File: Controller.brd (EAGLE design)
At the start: 125 x 65 mm, 38 parts, among them SW1 MULTICOLOR_BUTTON, SW2 MULTICOLOR_BUTTON, SW3 MULTICOLOR_BUTTON, SW4 MULTICOLOR_BUTTON, SW5 MULTICOLOR_BUTTON, SW6 MULTICOLOR_BUTTON, SW7 MULTICOLOR_BUTTON, SW8 MULTICOLOR_BUTTON, U1 ATMEGA328-PU, U2 DRV5053VAQLPGM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

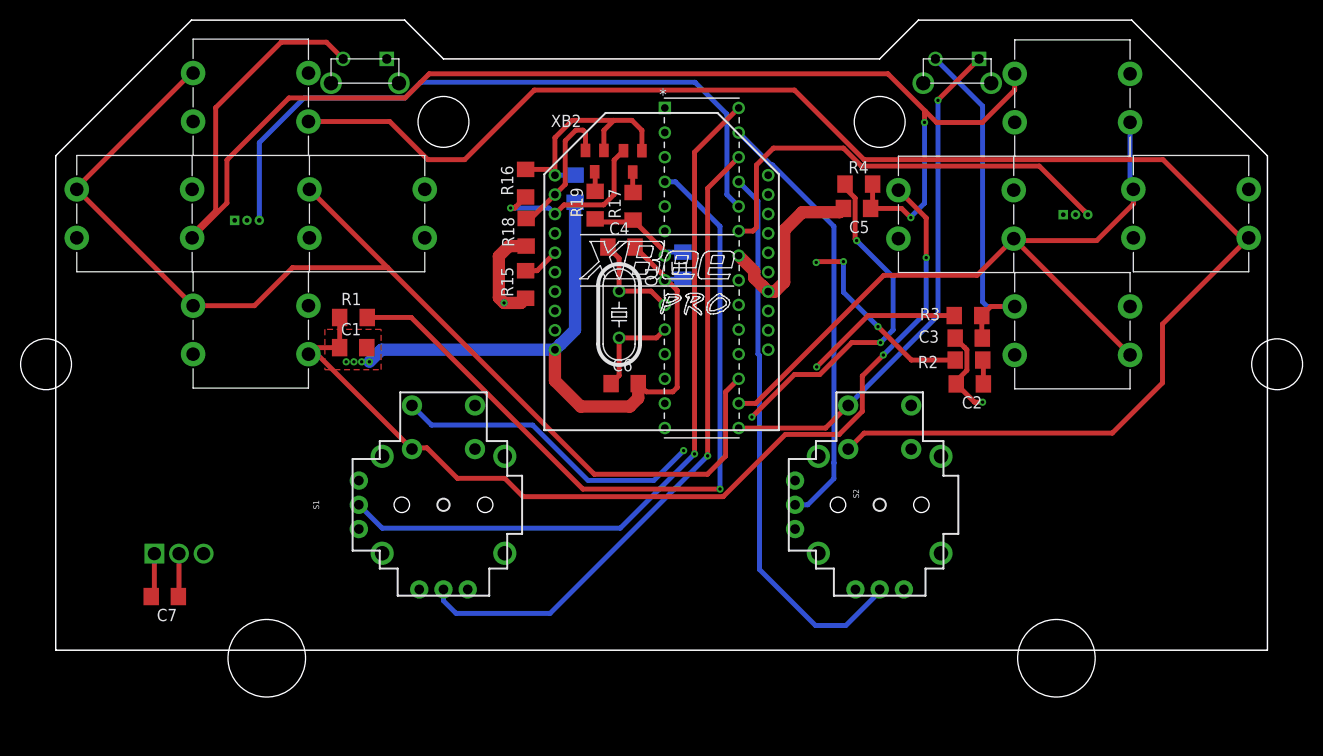
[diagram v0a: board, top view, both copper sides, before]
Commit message: added 5V regulator
Still need to add BMS circuitry and switch
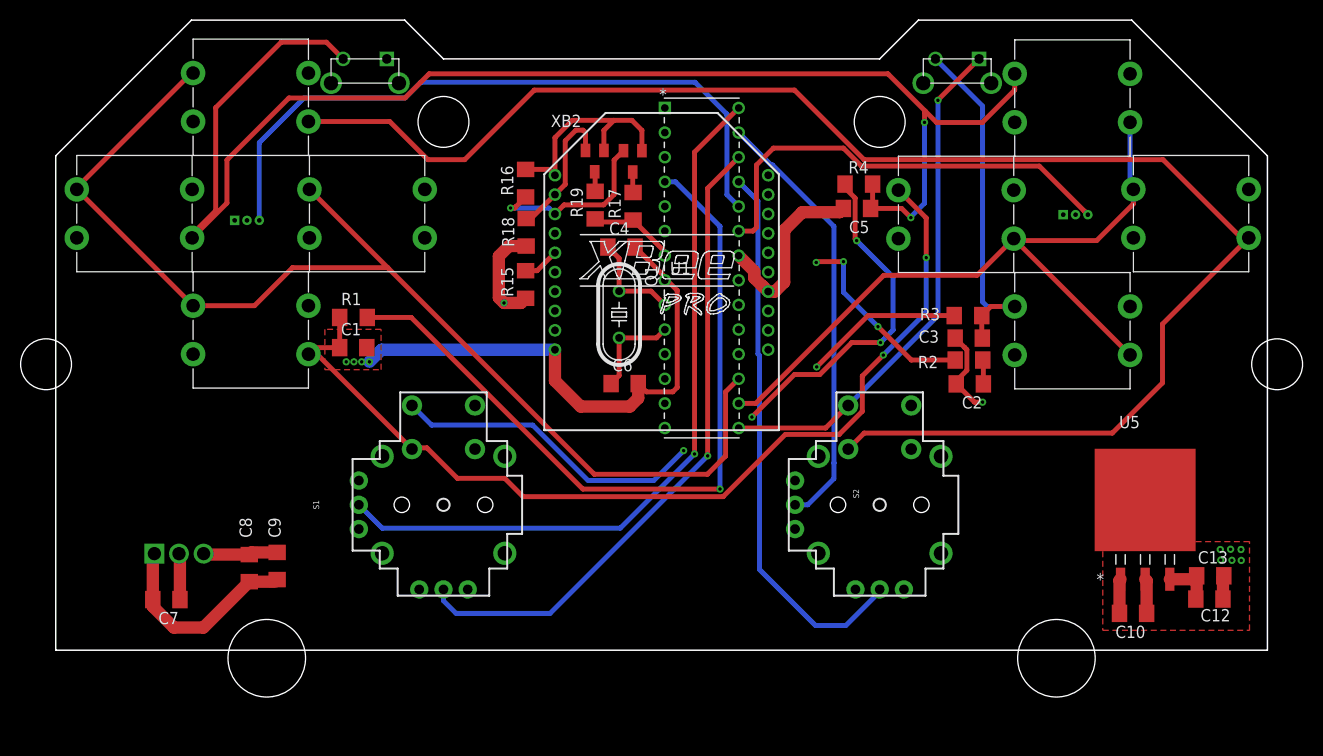
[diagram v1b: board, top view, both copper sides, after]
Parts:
- added C10, C12: 10u, rcl:C1206
- added C13: 0.1u, rcl:C1206
- added U5: LM1085ISX-5.0/NOPBTS3B-L, Controller:TS3B-L
- moved C8 54.5 mm to (20.0, 8.47), flipped to the top
- moved C9 49.6 mm to (22.8, 8.69), flipped to the top
- moved C7 0.35 mm to (11.4, 5.22)
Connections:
- new net VBAT: C12.1, C13.1, U5.3
- net +3V3: no longer C9.1
- net +5V: now also C10.1, C9.1, U5.2
- net GND: now also C10.2, C12.2, C13.2, U5.1
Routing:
- net +5V: track 91.4 -> 100.7 mm
- net VBAT: track 0.00 -> 5.36 mm
- net GND: track 115.5 -> 120.2 mm, vias 5 -> 11
- net +3V3: track 109.1 -> 107.4 mm

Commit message: rerouted so we only have 2 layers, added PWM pin
Need to add battery switch,indicator Vbat pins
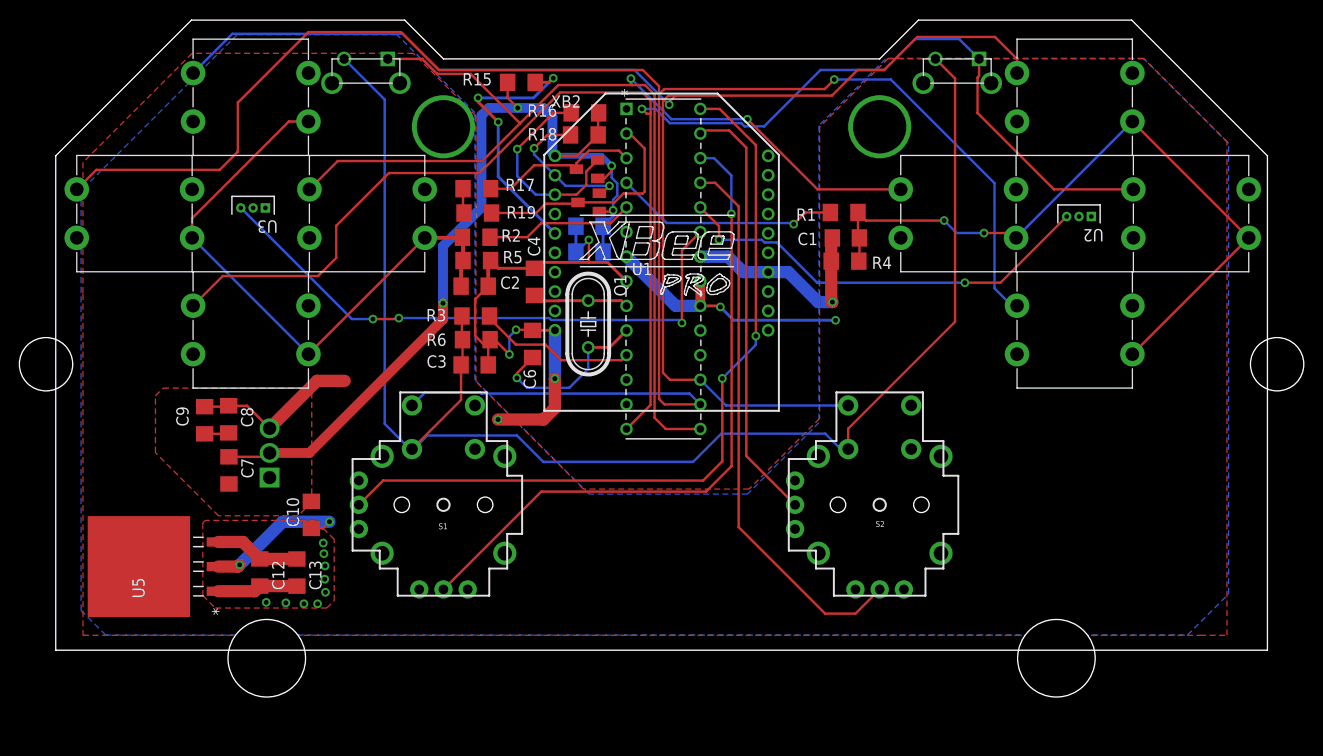
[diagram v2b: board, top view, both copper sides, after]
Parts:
- added C11: 0.1u, rcl:C1206
- added R5, R6: 100k, rcl:R1206
- C5: value 0.1u -> 10U
- moved U5 104.1 mm to (8.53, 8.62), turned to 90 degrees
- moved C12 98.0 mm to (21.1, 8.02), turned to 270 degrees
- moved SW1 97.7 mm to (117.0, 45.0)
- moved C13 94.2 mm to (24.9, 8.01), turned to 270 degrees
- moved SW2 88.3 mm to (105.0, 33.0)
- moved U3 87.4 mm to (19.1, 45.6), flipped to the top
- moved C10 85.4 mm to (26.4, 14.0), turned to 90 degrees
- moved SW8 85.0 mm to (20.0, 57.0), turned to 0 degrees
- moved U2 83.3 mm to (104.3, 44.7), flipped to the top
- moved SW7 74.0 mm to (32.0, 45.0), turned to 0 degrees
- moved R2 52.4 mm to (43.4, 42.6), turned to 0 degrees
- moved C2 52.1 mm to (43.2, 37.6), turned to 0 degrees
- moved C1 52.1 mm to (81.5, 42.5), turned to 180 degrees
- moved R1 51.8 mm to (81.3, 45.2), turned to 180 degrees
- moved C3 51.0 mm to (43.2, 29.4), turned to 0 degrees
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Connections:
- removed net $NC2: S2.B2A, SW2.4, SW6.4
- removed net AREF: U1.21
- removed net AVCC: U1.20
- removed net C4: R4.2, U1.14
- removed net N$C1: C1.1, R1.1, S1.B2A, SW1.4, SW5.4
- removed net N$C4: C5.1, R4.1, SW4.4, SW8.4, U$6.P$2
- new net $NC1: C1.1, R1.1, R4.1, SW1.4, SW2.4, SW5.4, SW6.4
- new net PWM: U1.12
- new net R4: S2.B1A, SW6.2, SW8.2, U1.17
- net +3V3: now also C11.1, C5.1
- net +5V: now also U1.20, U1.21
- net GND: now also C11.2, R4.2, R5.2, R6.2
- net N$C2: now also R5.1, SW3.4, SW4.4, SW7.4, SW8.4
- net N$C3: now also R6.1, S1.B2A, S2.B2A, U$6.P$2; no longer SW3.4, SW7.4
- net R1: now also U$4.P$1, U1.14; no longer SW2.2, SW4.2, U1.17
- net R2: now also U$6.P$1, U1.15; no longer SW6.2, SW8.2, U1.16
- net R3: now also SW2.2, SW4.2, U1.16; no longer S2.B1A, U$4.P$1, U$6.P$1, U1.15
- net RX: now also U1.2
- net TX: now also U1.3
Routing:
- net $NC2: track 161.8 -> 0.00 mm
- net N$C4: track 150.6 -> 0.00 mm, vias 2 -> 0
- net R4: track 0.00 -> 145.3 mm, vias 0 -> 1
- net N$C1: track 100.4 -> 0.00 mm, vias 2 -> 0
- net $NC1: track 0.00 -> 73.4 mm, vias 0 -> 2
- net R3: track 129.8 -> 193.2 mm, vias 2 -> 1
- net N$C2: track 2.49 -> 61.2 mm
- net N$C3: track 97.1 -> 154.8 mm
- net C1: track 78.4 -> 23.3 mm
- net R2: track 74.7 -> 128.7 mm, vias 0 -> 2
- net C4: track 44.8 -> 0.00 mm, vias 3 -> 0
- net R1: track 120.2 -> 159.7 mm, vias 0 -> 1
- net +5V: track 100.7 -> 62.4 mm, vias 0 -> 4
- net C2: track 50.0 -> 15.4 mm, vias 3 -> 0
- net GND: track 120.2 -> 92.3 mm, vias 11 -> 15
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- added copper zone on layer 1, net +5V
- added copper zone on layer 16, net GND
- removed copper zone on layer 2, net +5V
- removed copper zone on layer 15, net GND

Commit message: Added switch and LED
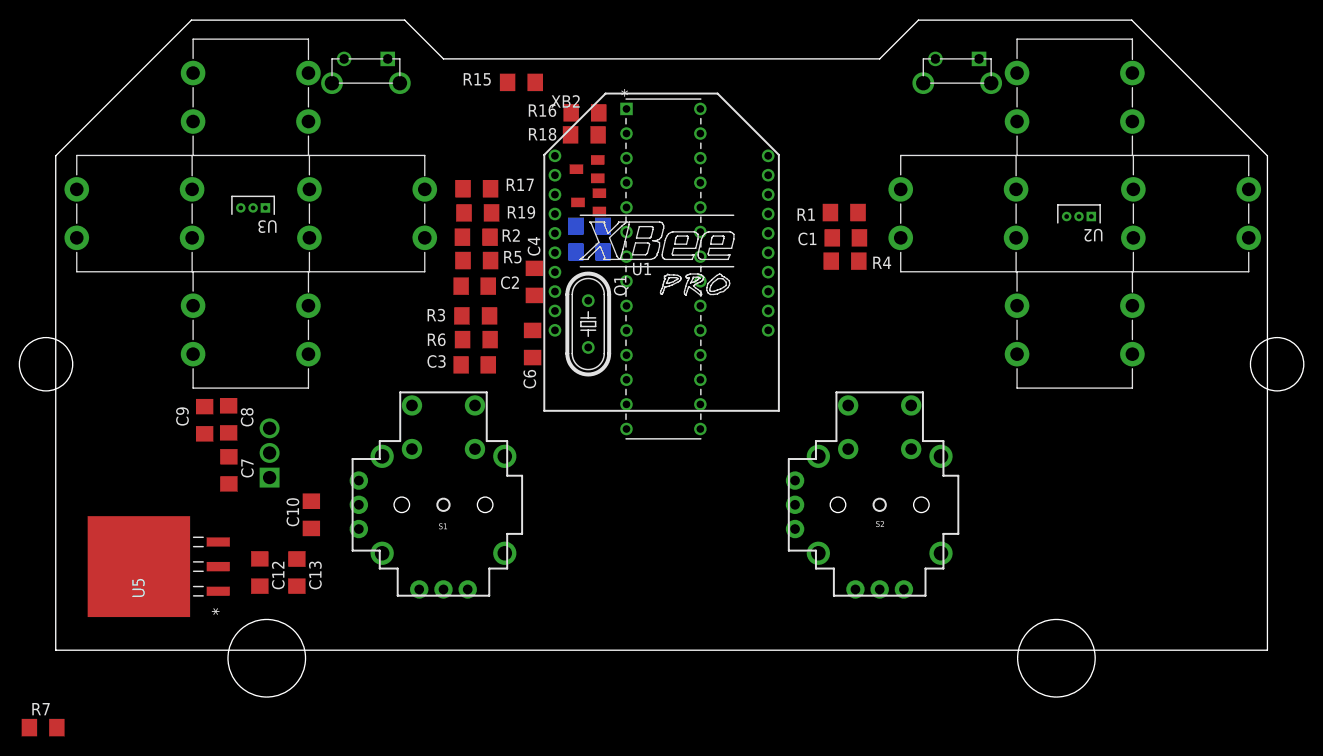
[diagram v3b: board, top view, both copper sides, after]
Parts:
- added R7: 1k, rcl:R1206
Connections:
- new net N$2: R7.2, U1.1
- net +5V: now also R7.1
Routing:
- net R3: track 193.2 -> 0.00 mm, vias 1 -> 0
- net R1: track 159.7 -> 0.00 mm, vias 1 -> 0
- net N$C3: track 154.8 -> 0.00 mm
- net R4: track 145.3 -> 0.00 mm, vias 1 -> 0
- net R2: track 128.7 -> 0.00 mm, vias 2 -> 0
- net +3V3: track 93.3 -> 0.00 mm, vias 4 -> 0
- net GND: track 92.3 -> 0.00 mm, vias 15 -> 0
- net X_LEFT: track 80.7 -> 0.00 mm, vias 2 -> 0
- net $NC1: track 73.4 -> 0.00 mm, vias 2 -> 0
- net Y_LEFT: track 68.9 -> 0.00 mm, vias 1 -> 0
- net +5V: track 62.4 -> 0.00 mm, vias 4 -> 0
- net N$C2: track 61.2 -> 0.00 mm
- net TRIGGER_RIGHT: track 60.7 -> 0.00 mm, vias 3 -> 0
- net Y_RIGHT: track 57.3 -> 0.00 mm
- net TRIGGER_LEFT: track 44.7 -> 0.00 mm, vias 2 -> 0
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- removed copper zone on layer 1, net +5V
- removed copper zone on layer 1, net GND
- removed copper zone on layer 16, net GND

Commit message: finished?
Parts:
- added J1: 282834-4, 282834-4:HDRV4W85P254_4X1_1062X650X1000
- added J2: 282834-2, 282834-2:CONN_282834-2
- added J3: 825457-3, 825457-3:TE_825457-3
- added R10: 150, rcl:R1206
- added R11: 475k, rcl:R1206
- added R12: 100k, rcl:R1206
- added R8, R9: 1k, rcl:R1206
- added SW9: 3PDT, Controller:3PDT
- added U$2: LED, Controller:R1206W
- added U$3: BSS138L, BSS138L:BSS138L
- added U6: (no value), Controller:SMD6
- C5: value 10U -> 10u
- moved R7 89.4 mm to (57.9, 59.0)
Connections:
- removed net N$2: R7.2, U1.1
- removed net VBAT: C12.1, C13.1, U5.3
- new net CLK: J3.3, U1.19
- new net MISO: J3.1, R9.2, U1.18
- new net MOSI: J3.4, R8.2, U1.17
- new net N$10: J1.2, SW9.P2, SW9.T32
- new net N$11: J1.3, SW9.P3
- new net N$12: SW9.T31, U6.P$3
- new net N$13: J2.1, R12.2, U6.P$1, U6.P$4
- new net N$15: SW9.T11, U6.P$6
- new net N$19: R11.2, R12.1, U6.P$2, U6.P$5
- new net N$5: U$4.P$3, U$6.P$3
- new net N$6: U$3.G, U1.6
- new net N$7: U$2.2, U$3.D
- new net N$8: R10.2, U$2.1
- new net N$9: J1.1, SW9.P1
- new net RESET: J3.5, R7.2, U1.1
- new net VCC: C12.1, C13.1, SW9.T12, U5.3
- net +5V: now also J3.2, R10.1, R8.1, R9.1, U5.4
- net GND: now also J1.4, J2.2, J3.6, R11.1, SW9.T21, U$3.S, U$4.P$4, U$6.P$4
- net R4: now also U1.13; no longer U1.17
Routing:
- net N$C3: track 0.00 -> 157.6 mm
- net R4: track 0.00 -> 148.6 mm
- net GND: track 0.00 -> 146.7 mm, vias 0 -> 2
- net CLK: track 0.00 -> 134.1 mm
- net R1: track 0.00 -> 130.2 mm, vias 0 -> 2
- net R3: track 0.00 -> 127.6 mm, vias 0 -> 1
- net +3V3: track 0.00 -> 109.3 mm, vias 0 -> 3
- net R2: track 0.00 -> 107.9 mm
- net RESET: track 0.00 -> 107.3 mm
- net +5V: track 0.00 -> 99.7 mm, vias 0 -> 55
- net $NC1: track 0.00 -> 78.7 mm
- net X_RIGHT: track 0.00 -> 76.2 mm
- net Y_RIGHT: track 0.00 -> 69.5 mm, vias 0 -> 2
- net MOSI: track 0.00 -> 69.3 mm, vias 0 -> 1
- net N$5: track 0.00 -> 66.9 mm, vias 0 -> 2
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- added copper zone on layer 1, net +5V
- added copper zone on layer 16, net +5V
- added copper zone on layer 16, net GND
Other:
- board text added: "+"
- board text added: "-"
- board text added: "BAT"
- board text added: "Charger"
- board text added: "ICSP"
- board text added: "PWM"

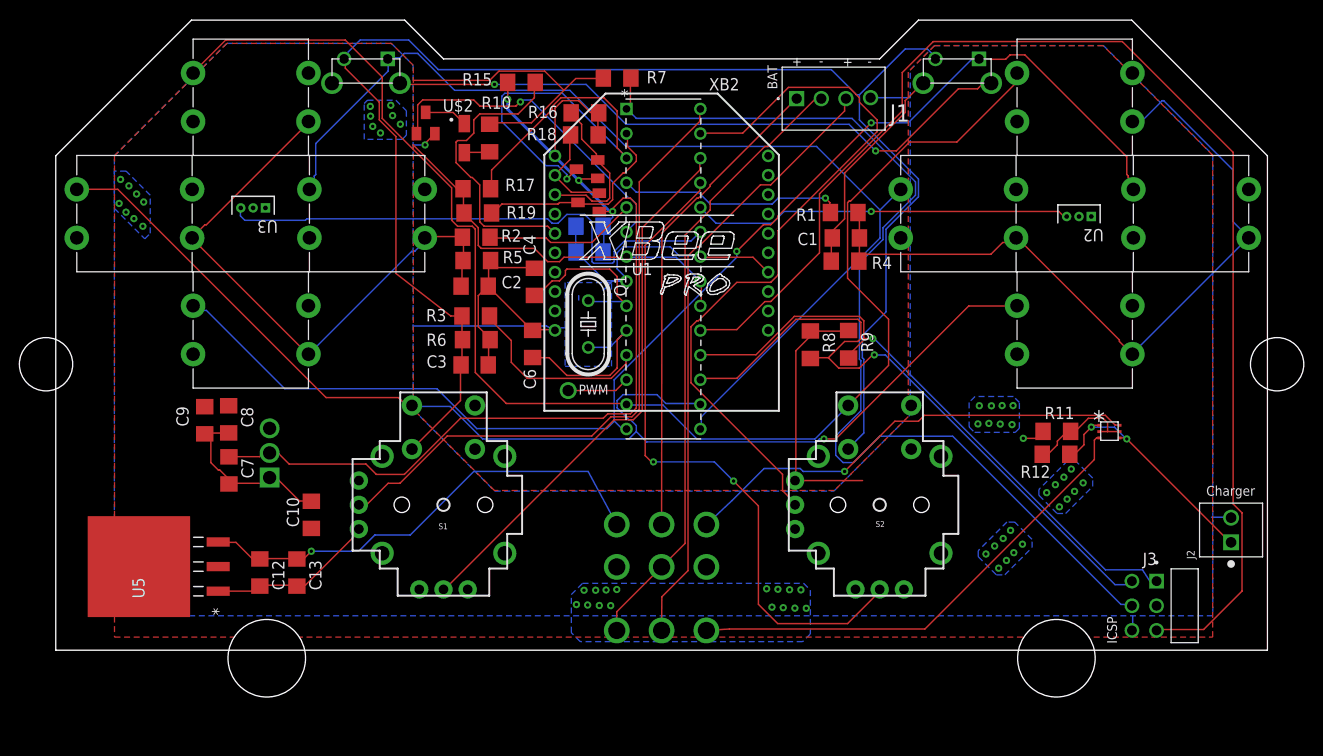
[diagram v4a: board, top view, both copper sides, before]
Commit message: Added diodes and made traces 10 mills
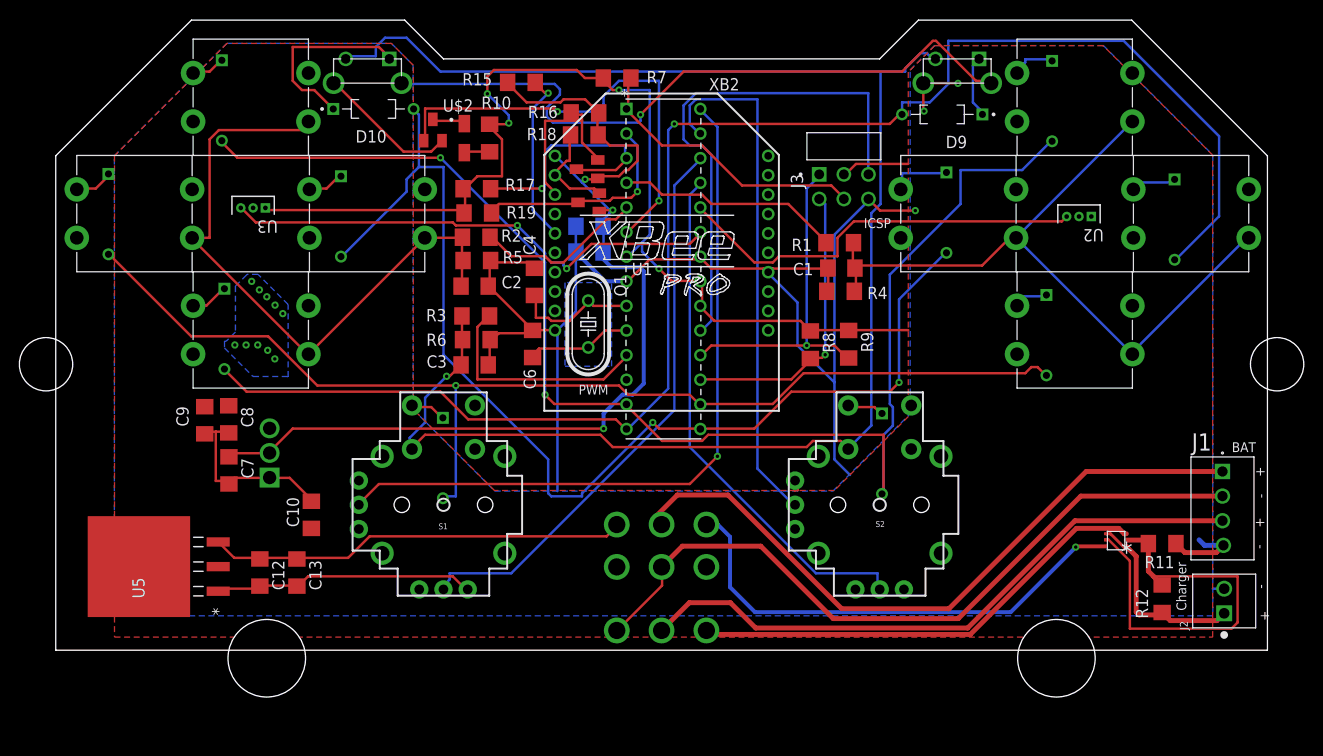
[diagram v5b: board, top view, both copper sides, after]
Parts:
- added D1, D10, D11, D12, D2, D3, D4, D5, D6, D7, D8, D9: 1N4148, 1N4148:DIOAD829W49L456D191
- moved J1 58.4 mm to (120.4, 18.4), turned to 270 degrees
- moved J3 54.5 mm to (78.8, 49.1), turned to 0 degrees
- moved R12 18.5 mm to (114.1, 5.31), turned to 270 degrees
- moved R11 15.9 mm to (114.1, 11.0), turned to 180 degrees
- moved U6 11.2 mm to (109.4, 11.4), turned to 180 degrees
- moved J2 7.36 mm to (120.5, 5.08)
- moved R1 3.15 mm to (80.9, 42.0)
- moved R4 3.15 mm to (81.0, 37.0)
- moved C1 3.15 mm to (81.0, 39.4)
- moved U$3 1.03 mm to (38.9, 53.7)
- moved U$6 0.16 mm to (32.2, 61.0)
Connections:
- new net N$16: D3.C, SW2.2
- new net N$18: D2.C, SW5.2
- new net N$2: D4.C, SW6.2
- new net N$20: D1.C, SW1.2
- new net N$21: D6.C, SW7.2
- new net N$22: D7.C, SW4.2
- new net N$23: D8.C, SW8.2
- new net N$24: D9.C, U$4.P$1
- new net N$25: D5.C, SW3.2
- new net N$26: D10.C, U$6.P$1
- new net N$27: D11.C, S1.B1A
- new net N$28: D12.C, S2.B1A
- net R1: now also D1.A, D5.A, D9.A; no longer SW1.2, SW3.2, U$4.P$1
- net R2: now also D10.A, D2.A, D6.A; no longer SW5.2, SW7.2, U$6.P$1
- net R3: now also D11.A, D3.A, D7.A; no longer S1.B1A, SW2.2, SW4.2
- net R4: now also D12.A, D4.A, D8.A; no longer S2.B1A, SW6.2, SW8.2
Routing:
- net CLK: track 134.1 -> 53.6 mm
- net RESET: track 107.3 -> 29.8 mm
- net GND: track 146.7 -> 210.9 mm, vias 2 -> 3
- net MOSI: track 69.3 -> 30.4 mm
- net N$19: track 11.8 -> 42.6 mm
- net MISO: track 63.9 -> 34.4 mm
- net R1: track 130.2 -> 159.5 mm, vias 2 -> 1
- net TX: track 53.3 -> 24.9 mm
- net N$9: track 49.8 -> 71.9 mm
- net X_RIGHT: track 76.2 -> 54.2 mm
- net +5V: track 99.7 -> 119.9 mm, vias 55 -> 14
- net N$26: track 0.00 -> 19.4 mm
- net Y_RIGHT: track 69.5 -> 54.3 mm, vias 2 -> 0
- net N$6: track 34.1 -> 46.5 mm, vias 1 -> 2
- net N$1: track 30.0 -> 17.9 mm, vias 0 -> 1
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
